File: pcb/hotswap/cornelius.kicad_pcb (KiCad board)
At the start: 2 copper layers, 271.8 x 128.2 mm, 126 parts, among them J1 AVR-ISP-6, SW1 SW_Push, U1 ATmega32U4-M, U2 PRTR5V0U2X, Y1 16MHz

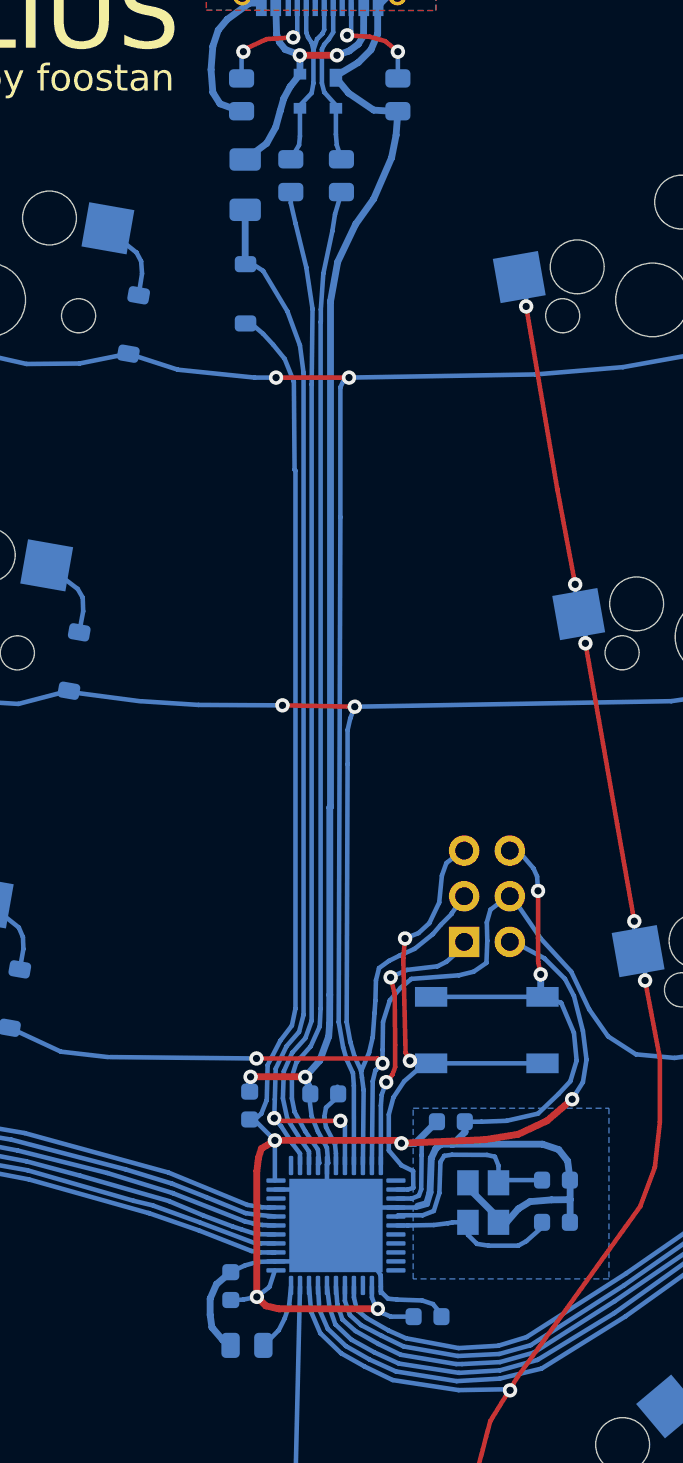
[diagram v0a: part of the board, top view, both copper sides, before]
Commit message: Fix pass capacitor
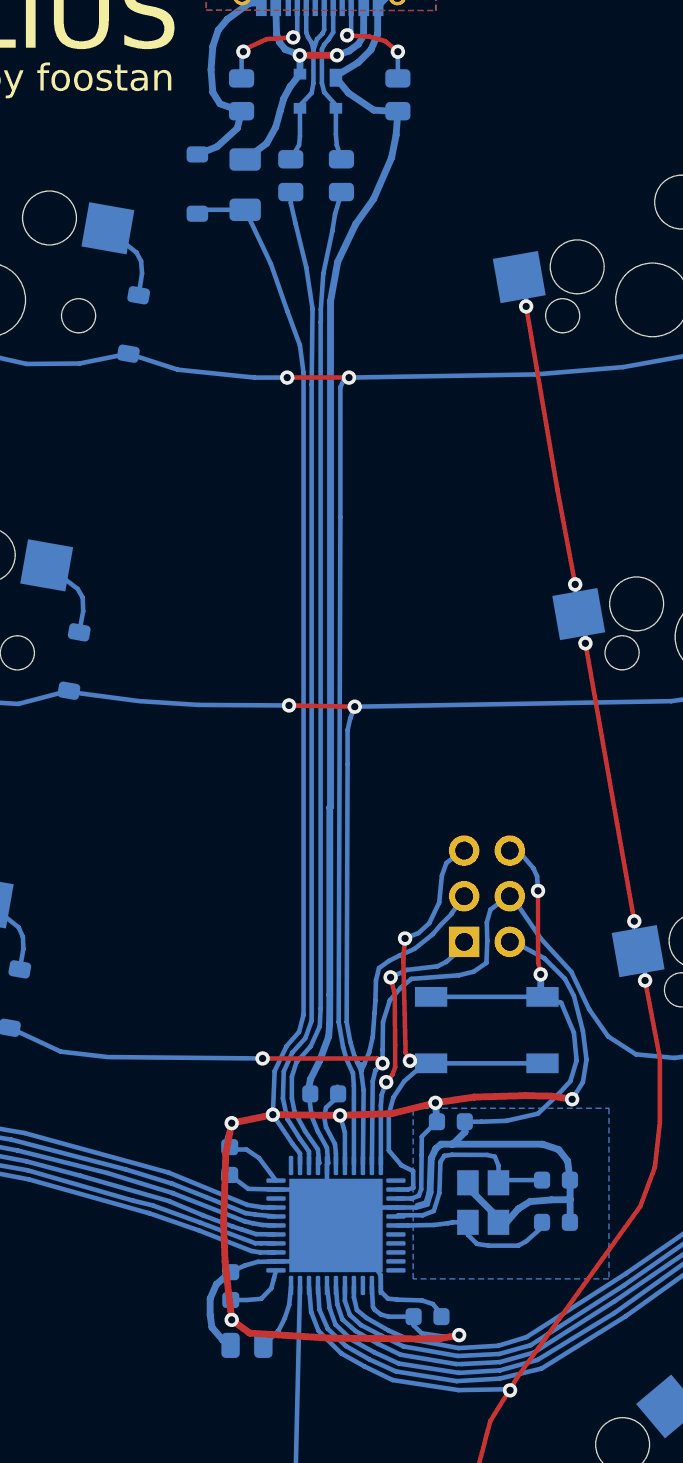
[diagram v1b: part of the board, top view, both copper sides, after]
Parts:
- moved ZD1 6.67 mm to (141.7, 58.0)
- moved C7 3.28 mm to (143.5, 112.3), turned to -90 degrees
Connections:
- F1 pad 1: VBUS -> +5V
- F1 pad 2: VCC -> VBUS
- U1 pad 2: VBUS -> +5V
- U1 pad 7: VBUS -> +5V
- U2 pad 4: VCC -> VBUS
- USB1 pad A4: VCC -> VBUS
- USB1 pad A9: VCC -> VBUS
- USB1 pad B4: VCC -> VBUS
- USB1 pad B9: VCC -> VBUS
- ZD1 pad 2: VBUS -> GND
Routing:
- net VBUS: track 61.4 -> 16.4 mm
- net +5V: track 109.7 -> 137.7 mm, vias 5 -> 7
- net VCC: track 16.4 -> 0.00 mm, vias 2 -> 0
- net GND: track 209.2 -> 211.8 mm, vias 4 -> 2
